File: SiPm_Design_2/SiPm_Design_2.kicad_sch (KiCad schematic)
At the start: 22 parts, among them IC4 AFBR-S4N44P014M, IC5 OPA2354AIDDARG3, J1 Conn_01x04_Pin, J2 Conn_Coaxial_Small

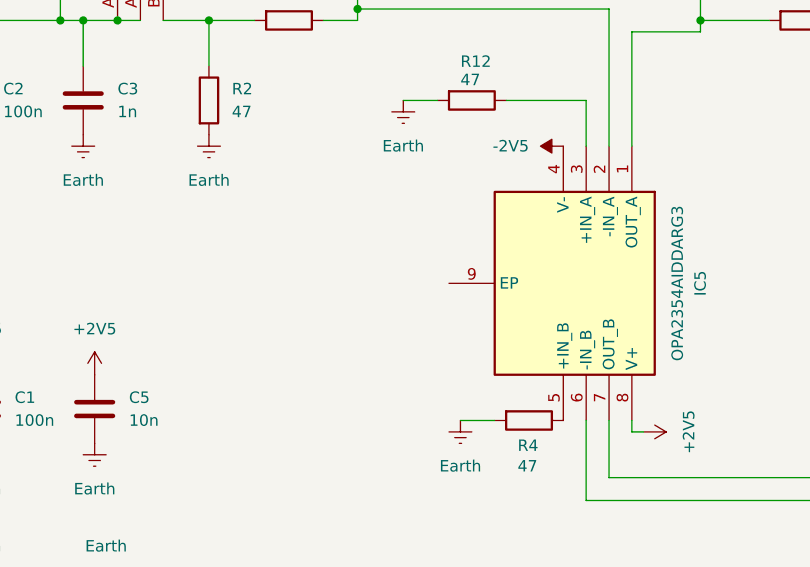
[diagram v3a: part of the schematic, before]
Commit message: add top fill, smaller font, SiPM hole
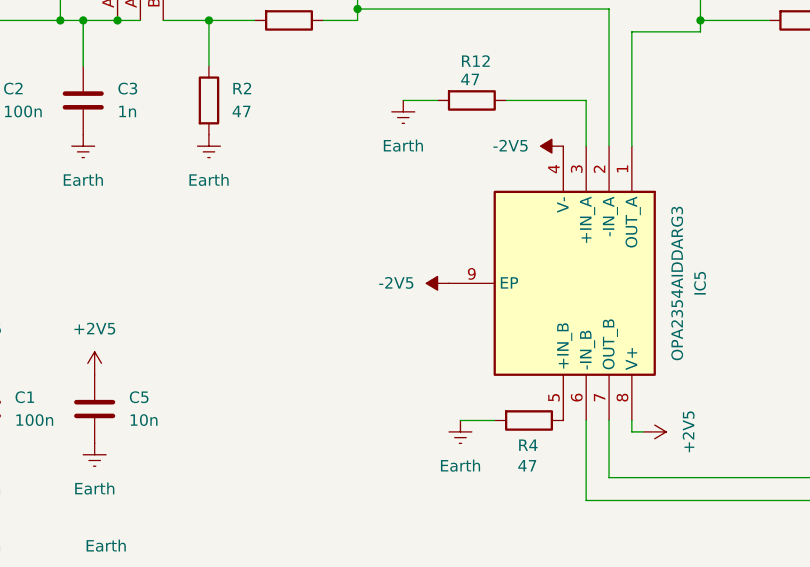
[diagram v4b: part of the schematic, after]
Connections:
- net -2V5: now also IC5.9 (EP)
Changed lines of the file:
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@@
+	)
+	(symbol
+		(lib_id "power:-2V5")
+		(at 137.16 130.81 90)
+		(unit 1)
+		(exclude_from_sim no)
+		(in_bom yes)
+		(on_board yes)
+		(dnp no)
+		(fields_autoplaced yes)
+		(property "Reference" "#PWR022"
+			(at 140.97 130.81 0)
+			(effects
+				(font
+					(size 1.27 1.27)
+				)
+				(hide yes)
+			)
+		)
+		(property "Value" "-2V5"
+			(at 133.35 130.8099 90)
+			(effects
+				(font
+					(size 1.27 1.27)
+				)
+				(justify left)
+			)
+		)
+		(property "Footprint" ""
+			(at 137.16 130.81 0)
+			(effects
+				(font
+					(size 1.27 1.27)
+				)
+				(hide yes)
+			)
+		)
+		(property "Datasheet" ""
+			(at 137.16 130.81 0)
+			(effects
+				(font
+					(size 1.27 1.27)
+				)
+				(hide yes)
+			)
+		)
+		(property "Description" "Power symbol creates a global label with name \"-2V5\""
+			(at 137.16 130.81 0)
+			(effects
+				(font
+					(size 1.27 1.27)
+				)
+				(hide yes)
+			)
+		)
+		(pin "1"
+		)
+		(instances
+			(project "SiPm_Design_2"
+				(path "/d64cfca3-4032-4a91-b47d-ee8cac34c76a"
+					(reference "#PWR022")
+					(unit 1)
+				)
+			)
+		)
 	)
 	(symbol

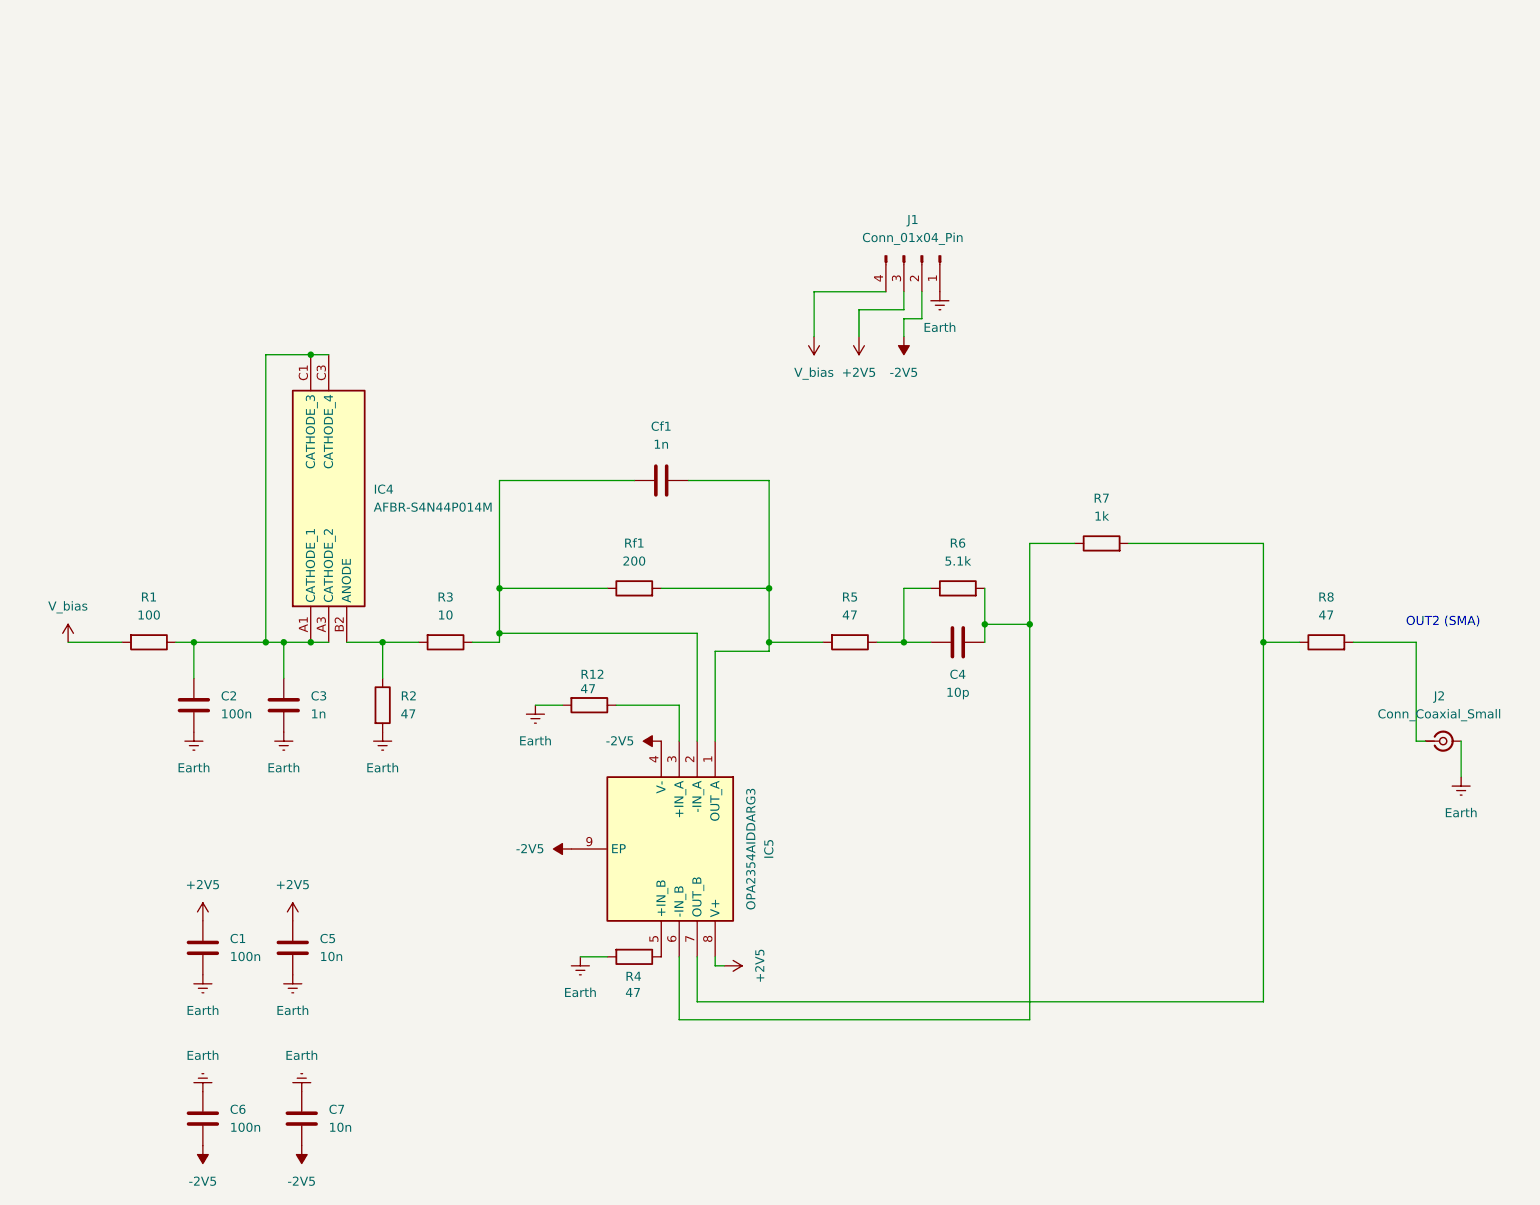
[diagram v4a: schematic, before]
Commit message: 1 Amp, flex , redesign
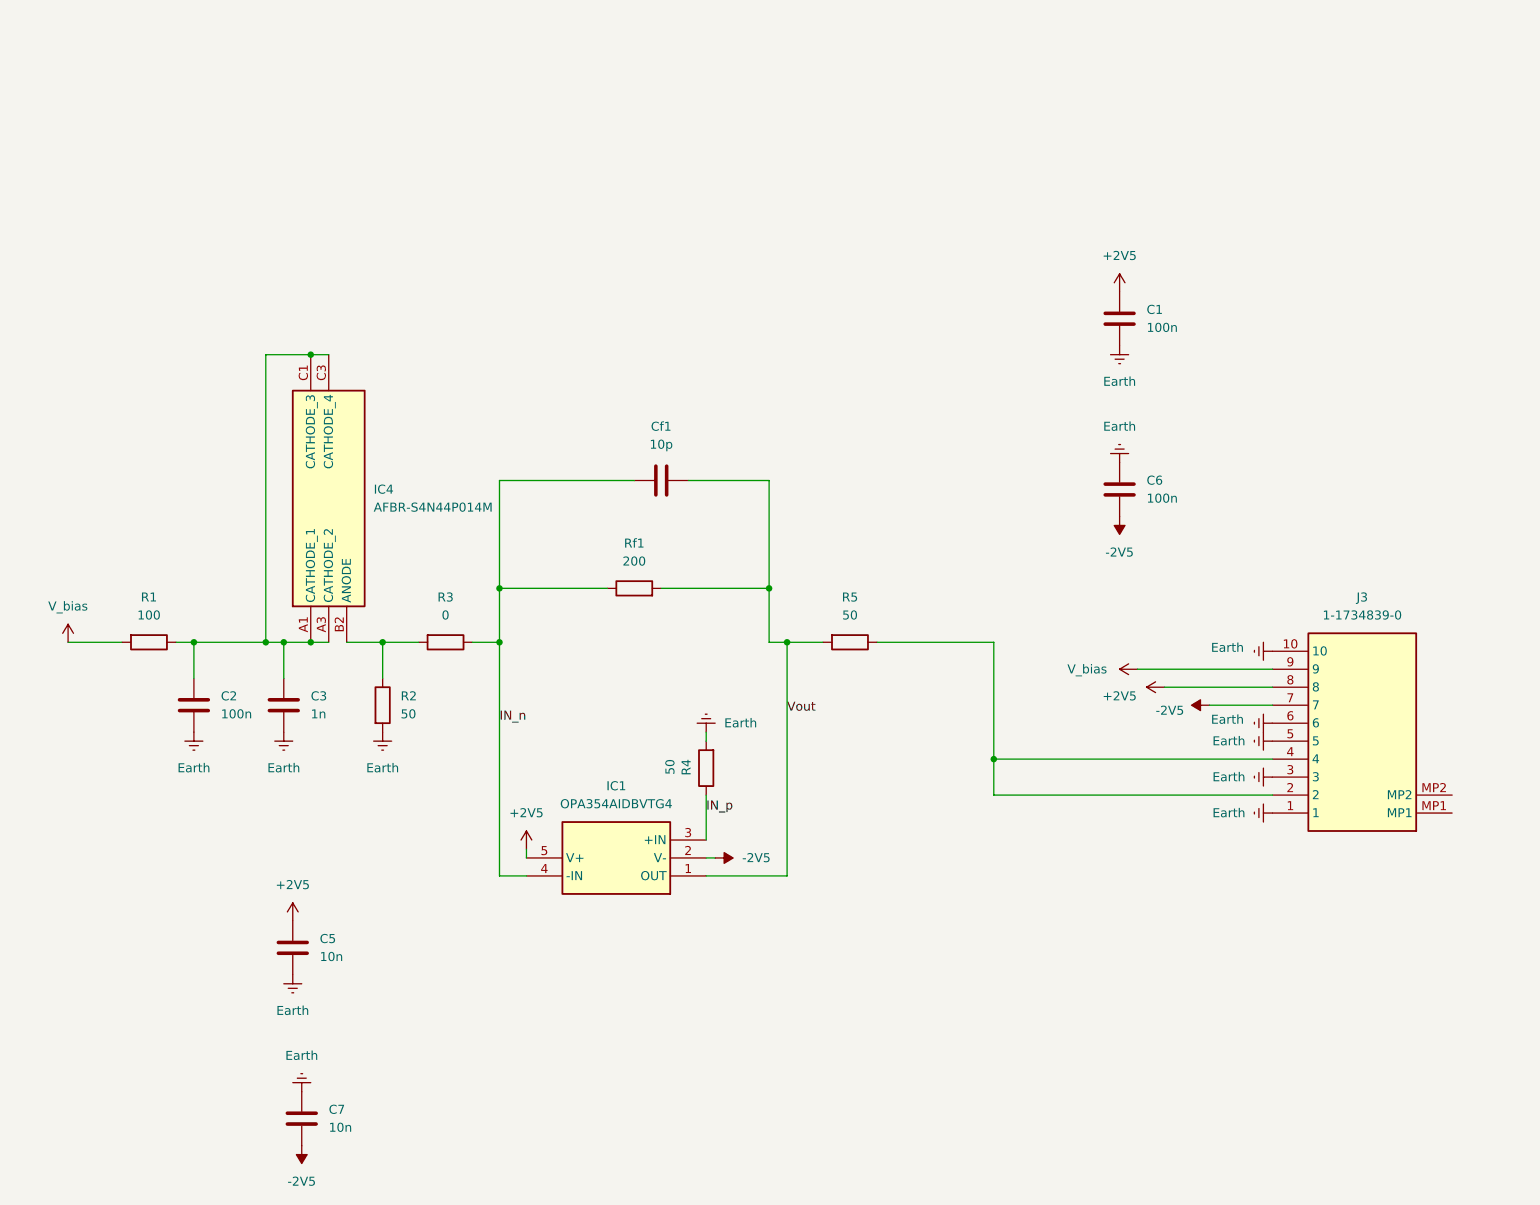
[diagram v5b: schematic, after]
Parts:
- removed C4: 10p, Capacitor_SMD:C_0603_1608Metric_Pad1.08x0.95mm_HandSolder, symbol Device:C
- removed IC5: OPA2354AIDDARG3, LIB_OPA2354AIDDARG3:SOIC127P600X170-9N, symbol OPA2354AIDDARG3:OPA2354AIDDARG3
- removed J1: Conn_01x04_Pin, Connector_Molex:Molex_KK-396_A-41792-0004_1x04_P3.96mm_Horizontal, symbol Connector:Conn_01x04_Pin
- removed J2: Conn_Coaxial_Small, Connector_Coaxial:SMA_Amphenol_901-143_Horizontal, symbol Connector:Conn_Coaxial_Small
- removed R12, R8: 47, Resistor_SMD:R_0603_1608Metric_Pad0.98x0.95mm_HandSolder, symbol Device:R
- removed R6: 5.1k, Resistor_SMD:R_0603_1608Metric_Pad0.98x0.95mm_HandSolder, symbol Device:R
- removed R7: 1k, Resistor_SMD:R_0603_1608Metric_Pad0.98x0.95mm_HandSolder, symbol Device:R
- added IC1: OPA354AIDBVTG4, SOT95P280X145-5N, symbol OPA354AIDBVTG4:OPA354AIDBVTG4
- added J3: 1-1734839-0, FPC 0.5 10P:117348390, symbol 1-1734839-0:1-1734839-0
- Cf1: value 1n -> 10p
- R2, R4, R5: value 47 -> 50
- R3: value 10 -> 0
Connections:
- net +2V5: now also IC1.5 (V+), J3.8
- net -2V5: now also IC1.2 (V-), J3.7
- net Earth: now also J3.1, J3.10, J3.3, J3.5, J3.6
- net V_bias: now also J3.9
- net at R5.1: now also J3.2, J3.4
- net IN_n: now reaches Cf1.1, R3.1, Rf1.1
- net IN_n: now also IC1.4 (-IN)
- net IN_p: now reaches R4.1
- net IN_p: now also IC1.3 (+IN)
- net Vout: now reaches Cf1.2, R5.2, Rf1.2
- net Vout: now also IC1.1 (OUT)
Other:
- note removed: "OUT2 (SMA)"
- moved on the sheet: C1, C6, R4

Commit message: ran through design rule
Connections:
- net Earth: now also J3.MP1, J3.MP2
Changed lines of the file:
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@@
+	)
+	(symbol
+		(lib_id "power:Earth")
+		(at 261.62 123.19 90)
+		(unit 1)
+		(exclude_from_sim no)
+		(in_bom yes)
+		(on_board yes)
+		(dnp no)
+		(fields_autoplaced yes)
+		(property "Reference" "#PWR024"
+			(at 267.97 123.19 0)
+			(effects
+				(font
+					(size 1.27 1.27)
+				)
+				(hide yes)
+			)
+		)
+		(property "Value" "Earth"
+			(at 265.43 123.1899 90)
+			(effects
+				(font
+					(size 1.27 1.27)
+				)
+				(justify right)
+			)
+		)
+		(property "Footprint" ""
+			(at 261.62 123.19 0)
+			(effects
+				(font
+					(size 1.27 1.27)
+				)
+				(hide yes)
+			)
+		)
+		(property "Datasheet" "~"
+			(at 261.62 123.19 0)
+			(effects
+				(font
+					(size 1.27 1.27)
+				)
+				(hide yes)
+			)
+		)
+		(property "Description" "Power symbol creates a global label with name \"Earth\""
+			(at 261.62 123.19 0)
+			(effects
+				(font
+					(size 1.27 1.27)
+				)
+				(hide yes)
+			)
+		)
+		(pin "1"
+		)
+		(instances
+			(project "SiPm_Design_2"
+				(path "/d64cfca3-4032-4a91-b47d-ee8cac34c76a"
+					(reference "#PWR024")
+					(unit 1)
+				)
+			)
+		)
 	)
 	(symbol
@@
 					(unit 1)
 				)
+			)
+		)
+	)
+	(symbol
+		(lib_id "power:Earth")
+		(at 261.62 125.73 90)
+		(unit 1)
+		(exclude_from_sim no)
+		(in_bom yes)
+		(on_board yes)
+		(dnp no)
+		(fields_autoplaced yes)
+		(property "Reference" "#PWR025"
+			(at 267.97 125.73 0)
+			(effects
+				(font
+					(size 1.27 1.27)
+				)
+				(hide yes)
+			)
+		)
+		(property "Value" "Earth"
+			(at 265.43 125.7299 90)
+			(effects
+				(font
+					(size 1.27 1.27)
+				)
+				(justify right)
+			)
+		)
+		(property "Footprint" ""
+			(at 261.62 125.73 0)
+			(effects
+				(font
+					(size 1.27 1.27)
+				)
+				(hide yes)
+			)
+		)
+		(property "Datasheet" "~"
+			(at 261.62 125.73 0)
+			(effects
+				(font
+					(size 1.27 1.27)
+				)
+				(hide yes)
+			)
+		)
+		(property "Description" "Power symbol creates a global label with name \"Earth\""
+			(at 261.62 125.73 0)
+			(effects
+				(font
+					(size 1.27 1.27)
+				)
+				(hide yes)
+			)
+		)
+		(pin "1"
+		)
+		(instances
+			(project "SiPm_Design_2"
+				(path "/d64cfca3-4032-4a91-b47d-ee8cac34c76a"
+					(reference "#PWR025")
+					(unit 1)
+				)

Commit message: gerber to JLC
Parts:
- added R6: 50, Resistor_SMD:R_0603_1608Metric_Pad0.98x0.95mm_HandSolder, symbol Device:R
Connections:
- net at J3.2, J3.4: now also R6.1; no longer R5.1
- new net: R5.1, R6.2
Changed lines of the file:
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@@
 	(wire
 		(pts
-			(xy 180.34 101.6) (xy 196.85 101.6)
+			(xy 180.34 101.6) (xy 184.15 101.6)
 		)
 		(stroke
@@
 	(wire
 		(pts
+			(xy 191.77 101.6) (xy 196.85 101.6)
+		)
+		(stroke
+			(width 0)
+			(type default)
+		)
+	)
+	(wire
+		(pts
 			(xy 153.67 78.74) (xy 165.1 78.74)
 		)
@@
 					(unit 1)
 				)
+			)
+		)
+	)
+	(symbol
+		(lib_id "Device:R")
+		(at 187.96 101.6 270)
+		(unit 1)
+		(exclude_from_sim no)
+		(in_bom yes)
+		(on_board yes)
+		(dnp no)
+		(fields_autoplaced yes)
+		(property "Reference" "R6"
+			(at 187.96 95.25 90)
+			(effects
+				(font
+					(size 1.27 1.27)
+				)
+			)
+		)
+		(property "Value" "50"
+			(at 187.96 97.79 90)
+			(effects
+				(font
+					(size 1.27 1.27)
+				)
+			)
+		)
+		(property "Footprint" "Resistor_SMD:R_0603_1608Metric_Pad0.98x0.95mm_HandSolder"
+			(at 187.96 99.822 90)
+			(effects
+				(font
+					(size 1.27 1.27)
+				)
+				(hide yes)
+			)
+		)
+		(property "Datasheet" "~"
+			(at 187.96 101.6 0)
+			(effects
+				(font
+					(size 1.27 1.27)
+				)
+				(hide yes)
+			)
+		)
+		(property "Description" "Resistor"
+			(at 187.96 101.6 0)
+			(effects
+				(font
+					(size 1.27 1.27)
+				)
+				(hide yes)
+			)
+		)
+		(pin "1"
+		)
+		(pin "2"
+		)
+		(instances
+			(project "SiPm_Design_2"
+				(path "/d64cfca3-4032-4a91-b47d-ee8cac34c76a"
+					(reference "R6")
+					(unit 1)
+				)

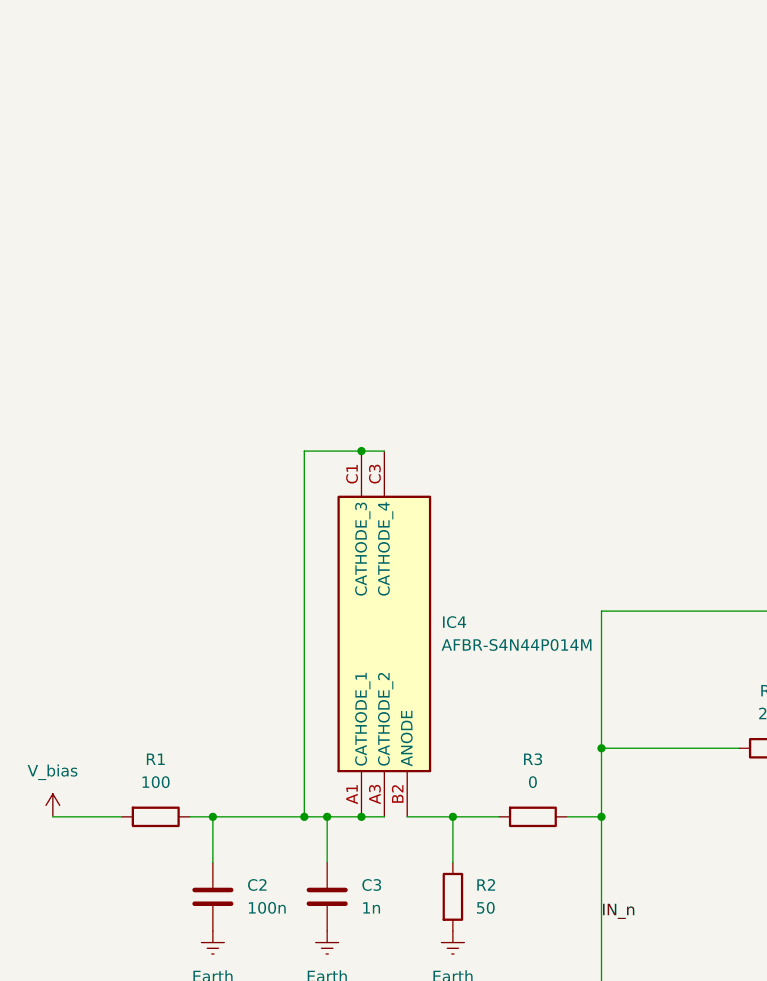
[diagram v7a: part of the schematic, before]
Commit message: extended SiPM section, 4 mirrored footprints.
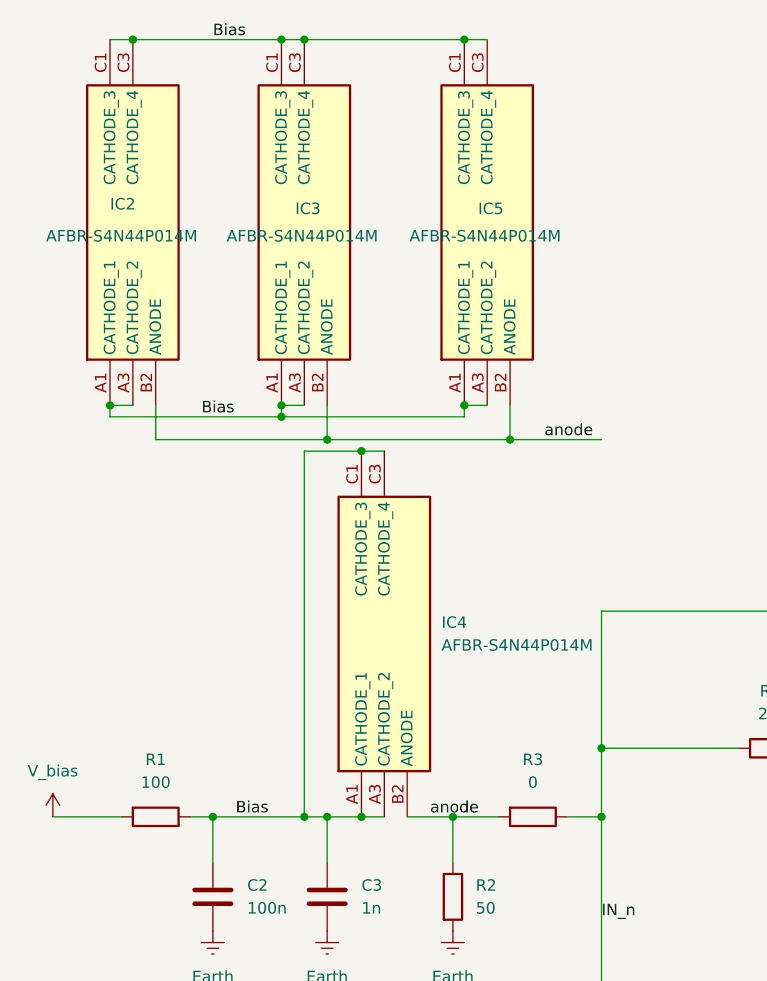
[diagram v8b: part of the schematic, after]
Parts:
- added IC2, IC3, IC5: AFBR-S4N44P014M, S4N44P014M:AFBRS4N44P014M, symbol AFBR-S4N44P014M:AFBR-S4N44P014M
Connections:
- net Bias: now reaches C2.1, C3.1, IC4.A1 (CATHODE_1), IC4.A3 (CATHODE_2), IC4.C1 (CATHODE_3), IC4.C3 (CATHODE_4), R1.1
- net Bias: now also IC2.A1 (CATHODE_1), IC2.A3 (CATHODE_2), IC2.C1 (CATHODE_3), IC2.C3 (CATHODE_4), IC3.A1 (CATHODE_1), IC3.A3 (CATHODE_2), IC3.C1 (CATHODE_3), IC3.C3 (CATHODE_4), IC5.A1 (CATHODE_1), IC5.A3 (CATHODE_2), IC5.C1 (CATHODE_3), IC5.C3 (CATHODE_4)
- net anode: now reaches IC4.B2 (ANODE), R2.1, R3.2
- net anode: now also IC2.B2 (ANODE), IC3.B2 (ANODE), IC5.B2 (ANODE)
